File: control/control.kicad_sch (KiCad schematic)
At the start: 0 parts

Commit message: SSD
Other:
- added sheet SSD (ssd.kicad_sch)
- sheet CM4IO ports: added PCIe_CK_N, PCIe_CK_P, PCIe_CK_nREQ, PCIe_RX_N, PCIe_RX_P, PCIe_TX_N, PCIe_TX_P, PCIe_nRST; removed none

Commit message: PSU
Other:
- added sheet power (power.kicad_sch)
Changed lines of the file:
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@@
+		)
+	)
+	(sheet
+		(at 16.51 15.24)
+		(size 31.75 38.1)
+		(stroke
+			(width 0.1524)
+			(type solid)
+		)
+		(fill
+			(color 0 0 0 0.0000)
+		)
+		(property "Sheetname" "power"
+			(at 17.018 17.272 0)
+			(effects
+				(font
+					(size 1.27 1.27)
+				)
+				(justify left bottom)
+			)
+		)
+		(property "Sheetfile" "power.kicad_sch"
+			(at 16.764 51.562 0)
+			(effects
+				(font
+					(size 1.27 1.27)
+				)
+				(justify left top)
+			)
+		)
+		(instances
+			(project "control"
+				(path "/f45f1ed7-9099-407f-b6ad-6cac15e7865f"
+					(page "4")
+				)
+			)
 		)
 	)

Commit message: Cleanup/organization
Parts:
- added J2: Screw_Terminal_01x03, TerminalBlock_TE-Connectivity:TerminalBlock_TE_282834-3_1x03_P2.54mm_Horizontal, symbol Connector:Screw_Terminal_01x03
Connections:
- new net Earth: J2.3 (Pin_3)
- new net LINE: J2.1 (Pin_1)
- new net NEUT: J2.2 (Pin_2)
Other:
- sheet CM4IO renamed CM4
- added sheet IO (io.kicad_sch)
- sheet CM4: file CM4IO.kicad_sch -> CM4.kicad_sch
- sheet CM4 ports: added +1V8, +3V3, +5V, GND; removed none
- sheet SSD ports: added +3V3, GND; removed none
- sheet power ports: added +5V, GND, LINE, NEUT; removed none

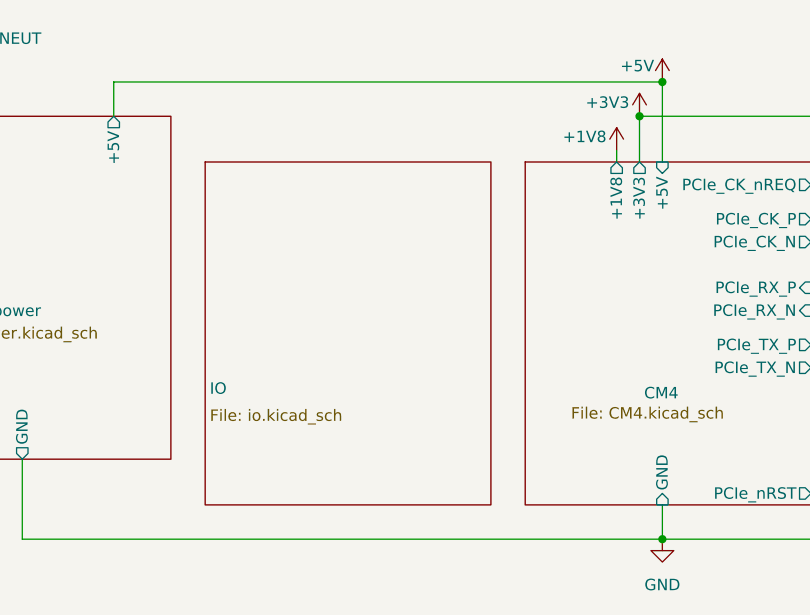
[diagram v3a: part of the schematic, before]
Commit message: Temp Sensor BME280 added to IO control
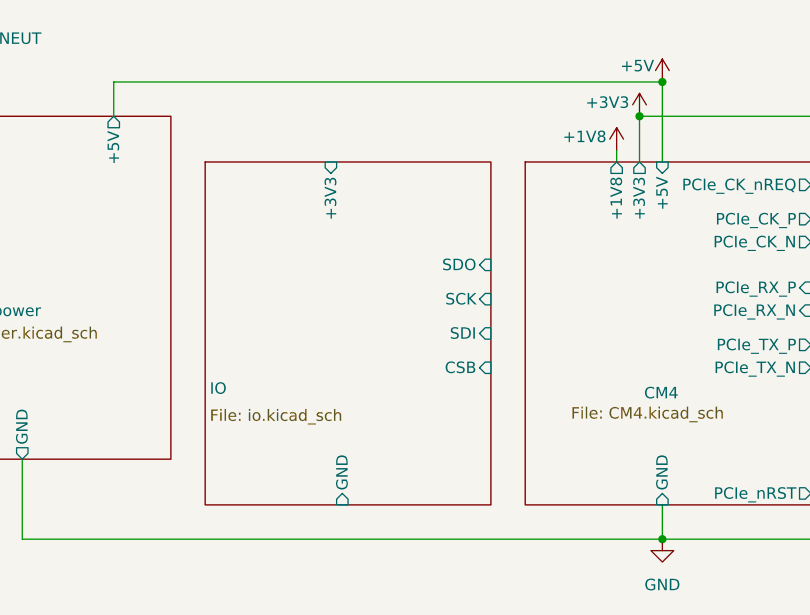
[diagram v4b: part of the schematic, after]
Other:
- sheet IO ports: added +3V3, CSB, GND, SCK, SDI, SDO; removed none
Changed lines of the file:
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@@
+			)
+		)
+		(pin "+3V3" input
+			(at 114.3 69.85 90)
+			(effects
+				(font
+					(size 1.27 1.27)
+				)
+				(justify right)
+			)
+		)
+		(pin "GND" input
+			(at 115.57 107.95 270)
+			(effects
+				(font
+					(size 1.27 1.27)
+				)
+				(justify left)
+			)
+		)
+		(pin "SDO" input
+			(at 132.08 81.28 0)
+			(effects
+				(font
+					(size 1.27 1.27)
+				)
+				(justify right)
+			)
+		)
+		(pin "SCK" input
+			(at 132.08 85.09 0)
+			(effects
+				(font
+					(size 1.27 1.27)
+				)
+				(justify right)
+			)
+		)
+		(pin "SDI" input
+			(at 132.08 88.9 0)
+			(effects
+				(font
+					(size 1.27 1.27)
+				)
+				(justify right)
+			)
+		)
+		(pin "CSB" input
+			(at 132.08 92.71 0)
+			(effects
+				(font
+					(size 1.27 1.27)
+				)
+				(justify right)
 			)
 		)

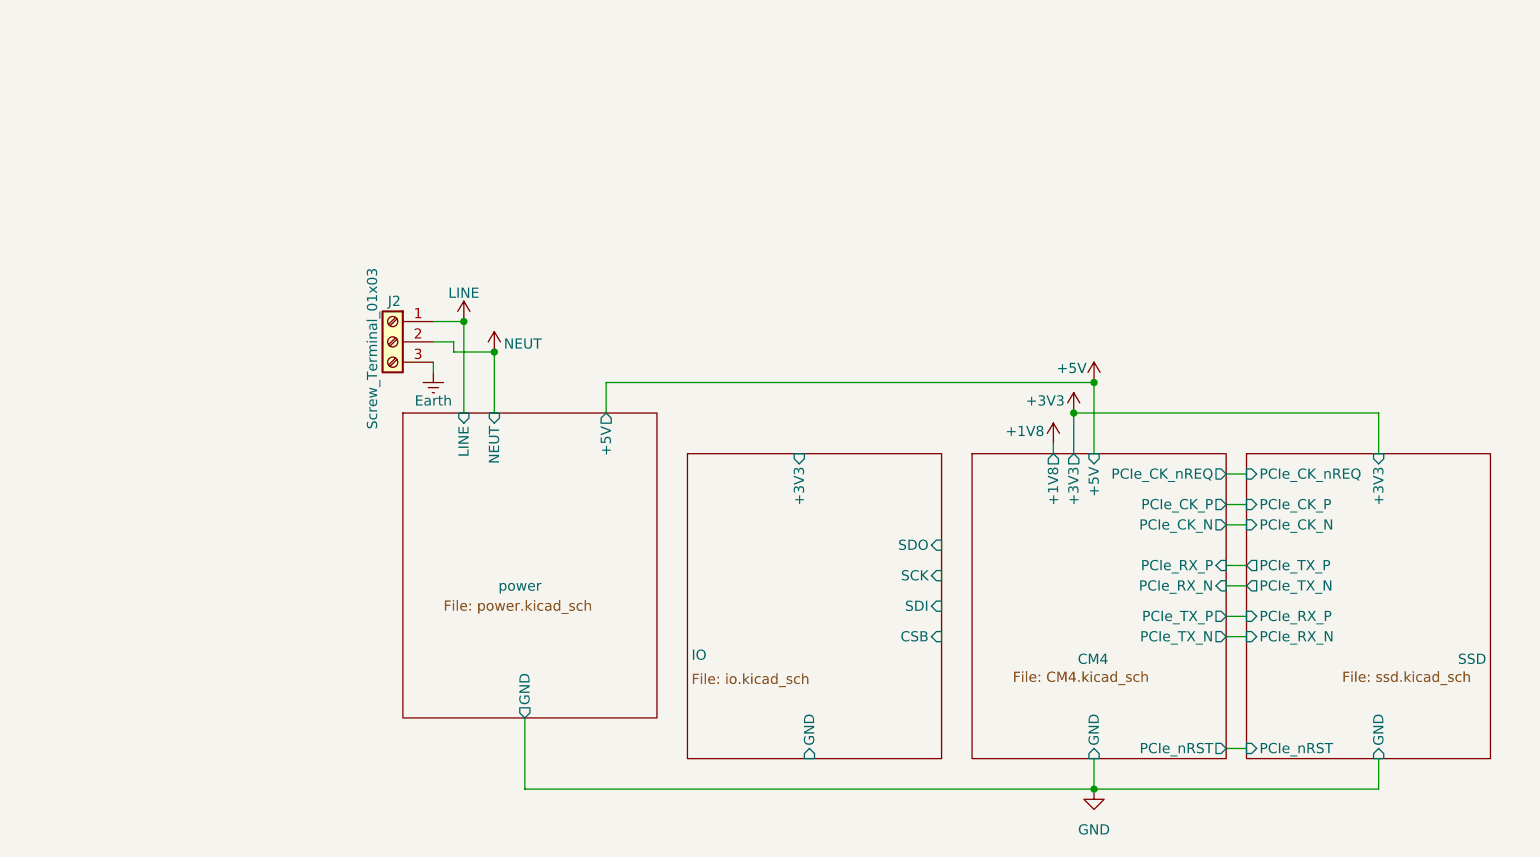
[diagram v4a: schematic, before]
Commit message: Component selection and BME280 cleanup
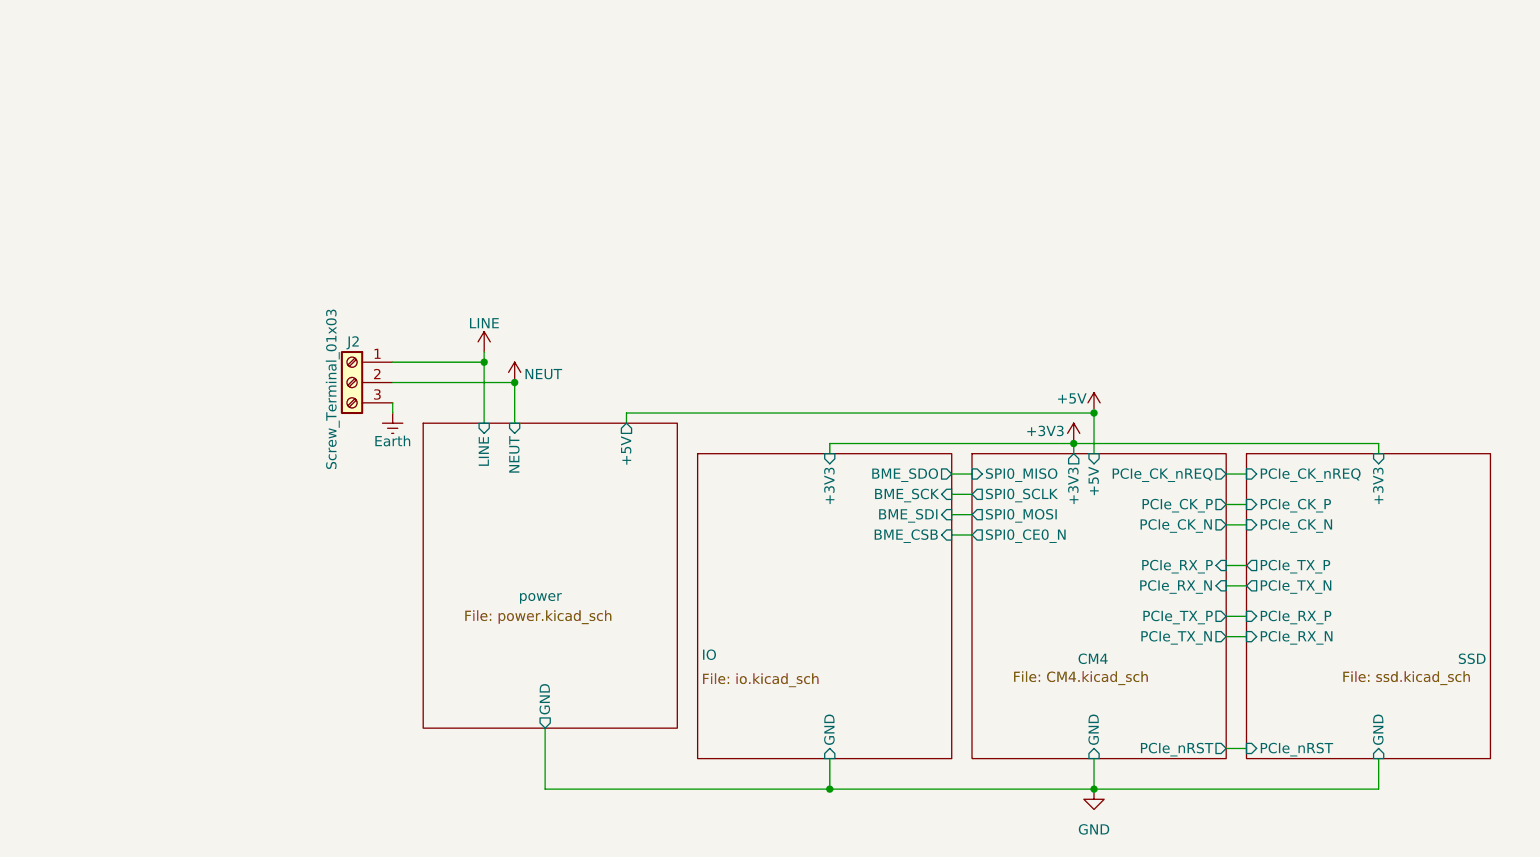
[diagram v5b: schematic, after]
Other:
- sheet CM4 ports: added SPI0_CE0_N, SPI0_MISO, SPI0_MOSI, SPI0_SCLK; removed +1V8
- sheet IO ports: added BME_CSB, BME_SCK, BME_SDI, BME_SDO; removed CSB, SCK, SDI, SDO
- moved on the sheet: J2

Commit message: Common PSU
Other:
- sheet power: file power.kicad_sch -> ../power.kicad_sch
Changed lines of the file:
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@@
 	)
 	(junction
-		(at 118.11 111.76)
+		(at 118.11 109.22)
 		(diameter 0)
 		(color 0 0 0 0)
@@
 	)
 	(junction
-		(at 151.13 111.76)
+		(at 151.13 109.22)
 		(diameter 0)
 		(color 0 0 0 0)
@@
 	(wire
 		(pts
-			(xy 151.13 107.95) (xy 151.13 111.76)
+			(xy 151.13 107.95) (xy 151.13 109.22)
 		)
 		(stroke
@@
 	(wire
 		(pts
-			(xy 118.11 107.95) (xy 118.11 111.76)
-		)
-		(stroke
-			(width 0)
-			(type default)
-		)
-	)
-	(wire
-		(pts
 			(xy 167.64 72.39) (xy 170.18 72.39)
 		)
@@
 	(wire
 		(pts
+			(xy 118.11 109.22) (xy 118.11 107.95)
+		)
+		(stroke
+			(width 0)
+			(type default)
+		)
+	)
+	(wire
+		(pts
 			(xy 186.69 68.58) (xy 148.59 68.58)
 		)
@@
 	(wire
 		(pts
-			(xy 82.55 111.76) (xy 118.11 111.76)
+			(xy 82.55 109.22) (xy 118.11 109.22)
 		)
 		(stroke
@@
 	(wire
 		(pts
-			(xy 186.69 111.76) (xy 186.69 107.95)
+			(xy 186.69 109.22) (xy 186.69 107.95)
 		)
 		(stroke
@@
 	(wire
 		(pts
-			(xy 118.11 111.76) (xy 151.13 111.76)
-		)
-		(stroke
-			(width 0)
-			(type default)
-		)
-	)
-	(wire
-		(pts
-			(xy 151.13 111.76) (xy 186.69 111.76)
+			(xy 118.11 109.22) (xy 151.13 109.22)
+		)
+		(stroke
+			(width 0)
+			(type default)
+		)
+	)
+	(wire
+		(pts
+			(xy 151.13 109.22) (xy 186.69 109.22)
 		)
 		(stroke
@@
 	(wire
 		(pts
-			(xy 82.55 104.14) (xy 82.55 111.76)
+			(xy 82.55 104.14) (xy 82.55 109.22)
 		)
 		(stroke
@@
 	(symbol
 		(lib_id "power:GND")
-		(at 151.13 111.76 0)
+		(at 151.13 109.22 0)
 		(unit 1)
 		(exclude_from_sim no)
@@
 		(fields_autoplaced yes)
 		(property "Reference" "#PWR024"
-			(at 151.13 118.11 0)
+			(at 151.13 115.57 0)
 			(effects
 				(font
@@
 		)
 		(property "Value" "GND"
-			(at 151.13 116.84 0)
+			(at 151.13 114.3 0)
 			(effects
 				(font
@@
 		)
 		(property "Footprint" ""
-			(at 151.13 111.76 0)
+			(at 151.13 109.22 0)
 			(effects
 				(font
@@
 		)
 		(property "Datasheet" ""
-			(at 151.13 111.76 0)
+			(at 151.13 109.22 0)
 			(effects
 				(font
@@
 		)
 		(property "Description" "Power symbol creates a global label with name \"GND\" , ground"
-			(at 151.13 111.76 0)
+			(at 151.13 109.22 0)
 			(effects
 				(font
@@
 			)
 		)
-		(property "Sheetfile" "power.kicad_sch"
+		(property "Sheetfile" "../power.kicad_sch"
 			(at 72.39 89.408 0)
 			(effects
